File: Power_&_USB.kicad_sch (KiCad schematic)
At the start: 23 parts, among them J5 USB4745-03-A, U12 SN74LVC1T45DCK, U4 FT232HPQ, U6 SN74AXC4T774RSVR

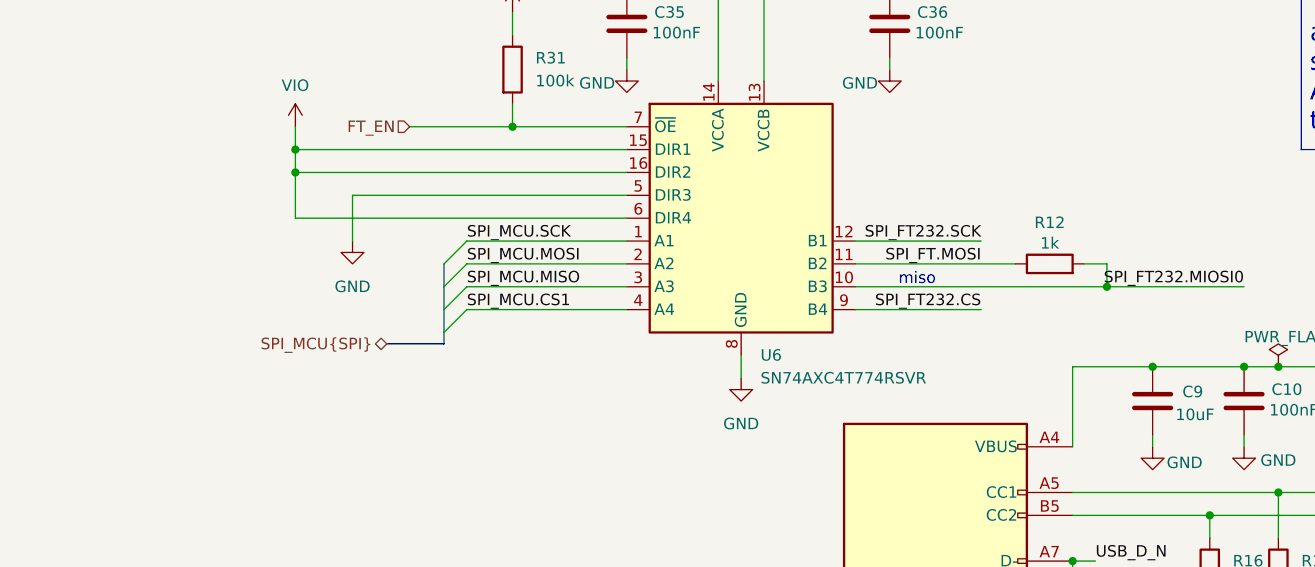
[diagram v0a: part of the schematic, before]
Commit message: new debug connector SOICbite, new board shape, new placement, addition of 22 ohm resistance in fast digital signals as spi
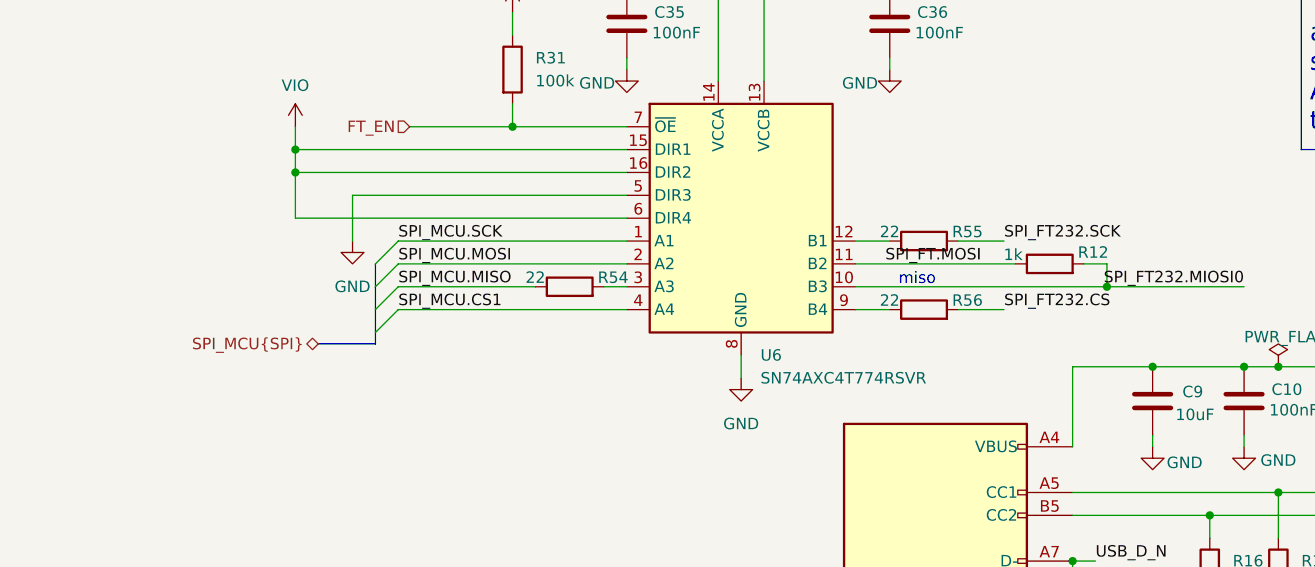
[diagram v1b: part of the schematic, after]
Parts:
- added R54, R55, R56: 22, Resistor_SMD:R_0201_0603Metric, symbol #dzdb:g_res/R-22-0201
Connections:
- net SPI_FT232.CS: now also R56.2; no longer U6.9 (B4)
- net SPI_FT232.SCK: now also R55.2; no longer U6.12 (B1)
- net SPI_MCU.MISO: now also R54.1; no longer U6.3 (A3)
- new net: R55.1, U6.12 (B1)
- new net: R54.2, U6.3 (A3)
- new net: R56.1, U6.9 (B4)

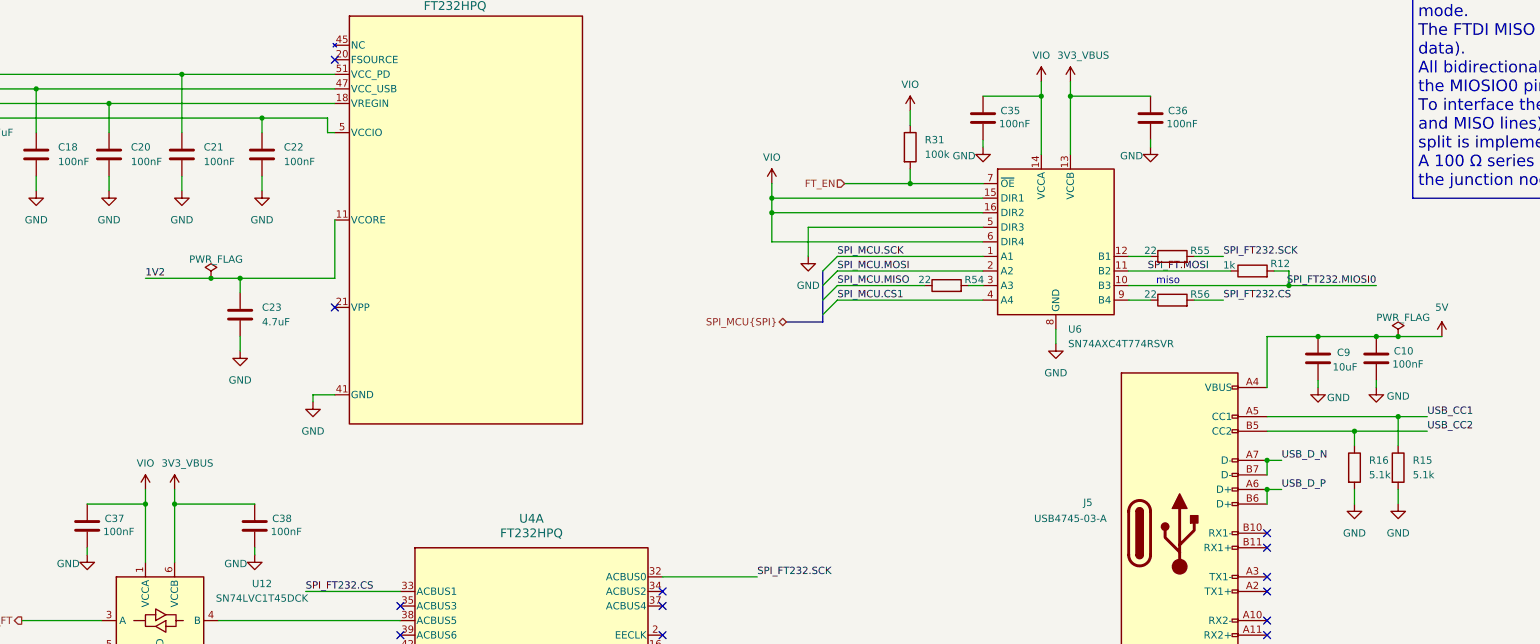
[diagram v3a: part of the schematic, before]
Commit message: updated routing SPI, change 0402 to 0201
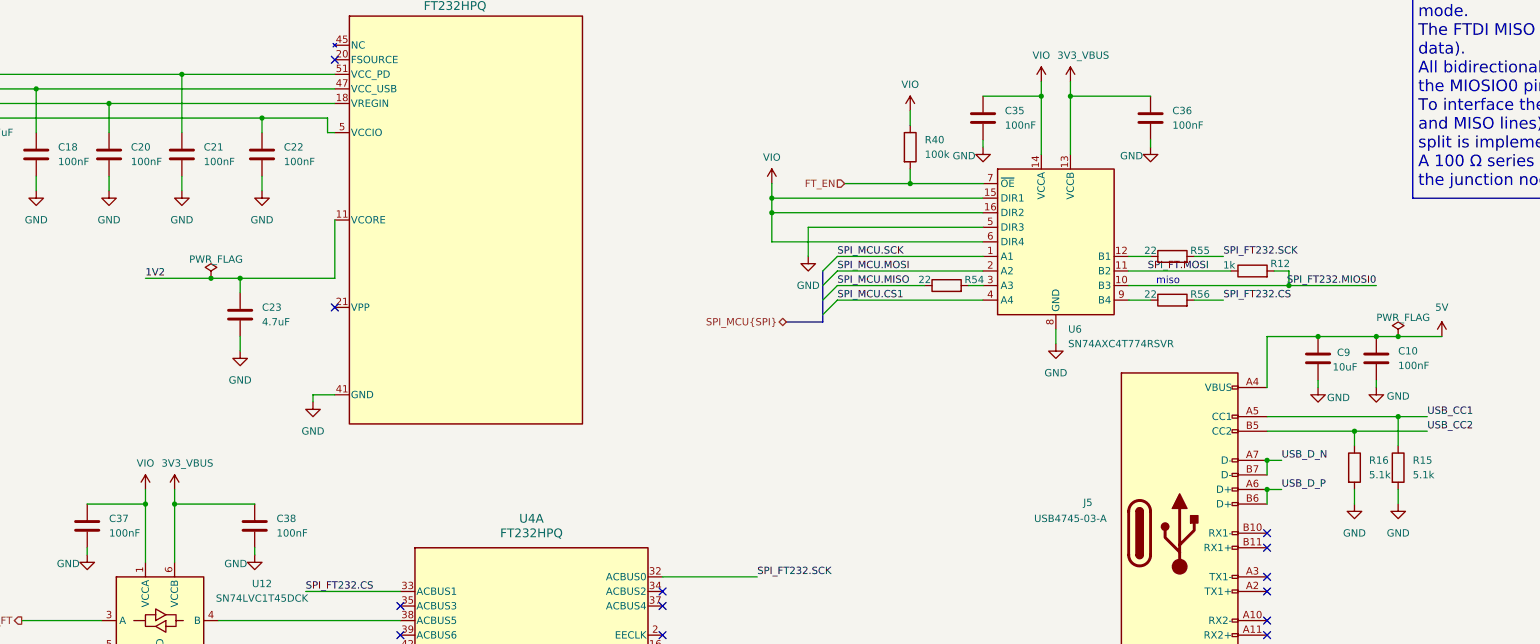
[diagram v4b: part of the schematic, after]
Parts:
- removed C10, C35, C36, C37, C38: 100nF, Capacitor_SMD:C_0603_1608Metric, symbol #dzdb:g_cap/C-100n-0603
- removed C18, C20, C21, C22: 100nF, Capacitor_SMD:C_0402_1005Metric, symbol #dzdb:g_cap/C-100n-0402
- removed R31: 100k, Resistor_SMD:R_0402_1005Metric, symbol #dzdb:g_res/R-100k-0402
- added C10, C18, C20, C21, C22, C35, C36, C37, C38: 100nF, Capacitor_SMD:C_0201_0603Metric, symbol #dzdb:g_cap/C-100n-0201
- added R40: 100k, Resistor_SMD:R_0201_0603Metric, symbol #dzdb:g_res/R-100K-0201
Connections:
- net 3V3_VBUS: now also C18.1, C20.1, C21.1, C22.1, C36.1, C38.1
- net 5V: now also C10.1
- net FT_EN: now also R40.2
- net GND: now also C10.2, C18.2, C20.2, C21.2, C22.2, C35.2, C36.2, C37.2, C38.2
- net VIO: now also C35.1, C37.1, R40.1

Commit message: Add comments from layout meeting 20.07.2026
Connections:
- net SPI_FT232.CS: now also U6.12 (B1); no longer R56.2
- net SPI_FT232.MIOSI0: now also R55.2; no longer U4.23 (ADBUS0)
- net SPI_FT232.SCK: now also R56.2; no longer R55.2
- net SPI_MCU.CS1: now also U6.1 (A1); no longer U6.4 (A4)
- net SPI_MCU.SCK: now also U6.4 (A4); no longer U6.1 (A1)
- net at R55.1: now also U4.23 (ADBUS0); no longer U6.12 (B1)
